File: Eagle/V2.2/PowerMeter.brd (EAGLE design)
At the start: 100 x 80 mm, 59 parts, among them IC1 4067D, IC2 4514D, X1 STEREOJACKSJ1-3525N, X10 STEREOJACK, X11 STEREOJACK, X12 STEREOJACK, X13 STEREOJACK, X14 STEREOJACK, X15 STEREOJACK, X16 STEREOJACK, X2 STEREOJACK, X3 STEREOJACK, X4 STEREOJACK, X5 STEREOJACK, X6 STEREOJACK, X7 STEREOJACK, X8 STEREOJACK, X9 STEREOJACK

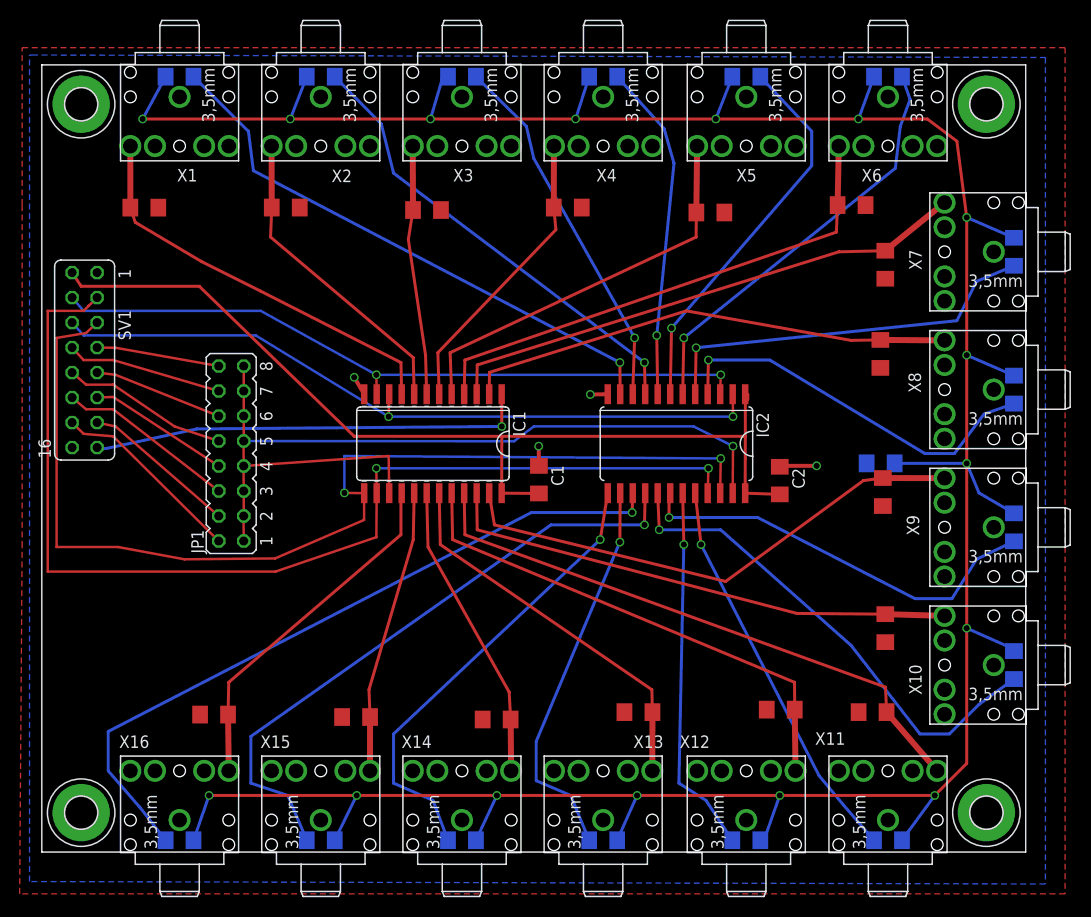
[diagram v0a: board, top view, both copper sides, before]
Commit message: Added V2.2 Eagle files and removed old versions due to hardware bug
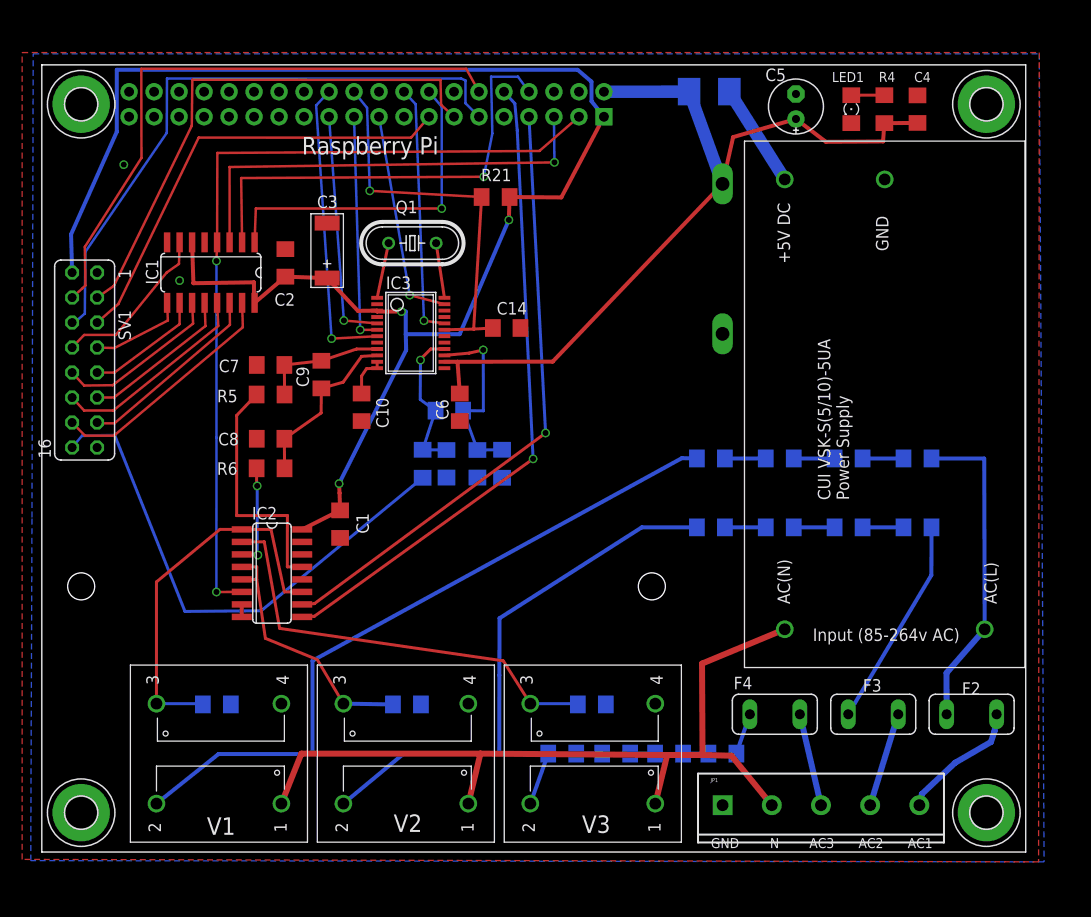
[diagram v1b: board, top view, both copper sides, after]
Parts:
- removed LED10, LED11, LED12, LED13, LED14, LED15, LED16, LED2, LED3, LED4, LED5, LED6, LED7, LED8, LED9: green, eagle-ltspice:LED_1206
- removed X10, X11, X12, X13, X14, X15, X16, X2, X3, X4, X5, X6, X7, X8, X9: STEREOJACK, adafruit:STX3100
- added C10, C14, C4, C6: .1uF, rcl:C1206
- added C11, C12, C7, C8: 220pF, rcl:C1206
- added C13, C9: 22nF, rcl:C1206
- added C3: 10u, Discrete:AVX-C
- added C5: 220uF, adafruit:E2,5-6E
- added D1: P6KE6.8A, diode:C1702-15
- added F1: 1.1A 6V, adafruit:1812
- added F2, F3, F4: MF-RM055/240-2, fuse:TE5
- added IC3: CS5463, Cirrus_Logic_By_element14_Batch_1:SSOP24
- added PS1: VSK-S10, CraigJensen:VSK-S10
- added Q1: 4.096MHz, crystal:HC49/S
- added R18: 59k, resistor:R1206
- added R19, R20: 1k, resistor:R1206
- added R21: 10K, resistor:R1206
- added T1, T2, T3: TV16E, CraigJensen:TV16E
- IC1: value 4067D -> 74HC138D; device 40xx:SO24W -> 74xx-eu:SO16
- IC2: value 4514D -> 4052D; device 45xx:SO24W -> 40xx:SO16
- JP1: value Board ID -> ACIN; device jumper:JP8Q -> SparkFun-Connectors:SCREWTERMINAL-5MM-5
- R1, R2, R3: value 5 -> 158
- R10, R11, R12, R13, R14, R15, R16, R7, R8, R9: value 5 -> 59k
- R17: value 120 -> 59k
- R4: value 5 -> 270
- R5, R6: value 5 -> 1k
- SV1: value (none) -> Current Brd Connector
- X1: value STEREOJACKSJ1-3525N -> RASPI_BOARD_B+_E4; device adafruit:STX3100 -> raspberrypi_bastelstube_v13:RASPI_BOARD_B+_EDGES_4DRILL
- moved H1 92.0 mm to (96.0, 76.0)
- moved H3 92.0 mm to (4.00, 4.00)
- moved X1 77.4 mm to (65.5, 23.5), flipped to the bottom, turned to 0 degrees
- moved R16 74.0 mm to (89.0, 33.0), flipped to the bottom, turned to 0 degrees
- moved H2 72.0 mm to (96.0, 4.00)
- moved H4 72.0 mm to (4.00, 76.0)
- moved LED1 68.3 mm to (82.3, 75.5), flipped to the top, turned to 270 degrees
- moved R6 64.8 mm to (23.2, 39.0), turned to 180 degrees
- moved JP1 62.2 mm to (66.7, 0.30), turned to 0 degrees
- moved C2 54.9 mm to (24.8, 59.9)
- moved R3 53.0 mm to (55.9, 15.0), flipped to the bottom
- moved R2 52.0 mm to (37.1, 15.0), flipped to the bottom
- moved R1 51.0 mm to (17.8, 15.0), flipped to the bottom
- moved R5 48.4 mm to (23.2, 46.5), turned to 180 degrees
- moved IC2 43.2 mm to (23.4, 28.3), turned to 270 degrees
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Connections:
- removed net N$22: IC1.8, R2.1, X2.5
- removed net N$24: IC1.6, R4.1, X4.5
- removed net N$25: IC1.4, R6.1, X6.5
- removed net N$26: IC1.3, R7.1, X7.5
- removed net N$28: IC1.2, R8.1, X8.5
- removed net N$29: IC1.23, R9.1, X9.5
- removed net N$30: IC2.14, LED13.A
- removed net N$32: IC2.19, LED12.A
- removed net N$34: IC2.20, LED11.A
- removed net N$36: IC2.17, LED10.A
- removed net N$40: IC2.4, LED8.A
- removed net N$42: IC2.5, LED7.A
- removed net N$44: IC2.6, LED6.A
- removed net N$48: IC2.8, LED4.A
- removed net N$50: IC1.22, R10.1, X10.5
- removed net N$51: IC1.21, R11.1, X11.5
- removed net N$52: IC2.10, LED3.A
- removed net N$54: IC2.9, LED2.A
- removed net N$56: IC2.11, LED1.A
- removed net N$58: IC1.20, R12.1, X12.5
- removed net N$59: IC1.18, R14.1, X14.5
- removed net N$60: IC1.17, R15.1, X15.5
- removed net N$66: IC1.19, R13.1, X13.5
- removed net N$68: IC1.16, R16.1, X16.5
- removed net VDD: C1.2, C2.2, IC1.24, IC2.1, IC2.24, SV1.2
- new net +3V3: C1.2, C2.2, C3.+, IC1.16, IC1.6, IC2.16, IC3.3, R21.1, SV1.2, X1.1
- new net +5V: F1.2, PS1.P$3
- new net 5V: C4.2, C5.+, C6.2, D1.C, F1.1, IC3.14, R4.1, X1.2
- new net AC(L): F2.1, PS1.P$2, R18.1
- new net AC(N): JP1.2, PS1.P$1, T1.1, T2.1, T3.1
- new net BS-0: IC1.15, SV1.14
- new net BS-1: IC1.14, SV1.13
- new net BS-2: IC1.13, SV1.12
- new net BS-3: IC1.12, SV1.11
- new net BS-4: IC1.11, SV1.10
- new net BS-5: IC1.10, SV1.9
- new net BS-6: IC1.9, SV1.7
- new net BS-7: IC1.7, SV1.8
- new net BS-A: IC1.1, X1.16
- new net BS-B: IC1.2, X1.8
- new net BS-C: IC1.3, X1.5
- new net C5: C12.1, C13.1, IC3.16, R20.2
- new net CS: IC3.7, X1.24
- new net CS-A: SV1.6, X1.11
- new net CS-B: SV1.4, X1.12
- new net CS-C: SV1.3, X1.13
- new net CS-D: SV1.5, X1.15
- new net IIN+: R20.1, SV1.16
- new net INH: IC1.4, IC2.6, X1.3
- new net INT: IC3.20, X1.18
- new net N$39: IC2.3, R6.2
- new net R1: C7.2, C9.2, IC3.9, R5.1
- new net RESET: C14.2, IC3.19, R21.2, X1.22
- new net SCLK: IC3.5, X1.23
- new net SDI: IC3.23, X1.19
- new net SDO: IC3.6, X1.21
- new net VIN-1: IC2.1, IC2.11, R1.2, T1.4
- new net VIN-2: IC2.4, IC2.5, R2.2, T2.4
- new net VIN-3: IC2.2, R3.2, T3.4
- new net VS-A: IC2.10, X1.7
- new net VS-B: IC2.9, X1.10
- net GND: now also C10.1, C11.1, C12.2, C14.1, C3.-, C4.1, C5.-, C6.1, C7.1, C8.2, D1.A, IC1.5, IC1.8, IC2.14, IC2.15, IC2.7, IC2.8, IC3.13, IC3.4, IC3.8, JP1.1, LED1.C, PS1.P$4, R1.1, R19.1, R2.1, R3.1, SV1.15, T1.3, T2.3, T3.3, X1.6; no longer IC1.12, R17.1
- net N$1: now also IC3.1, Q1.1; no longer IC1.10, IC2.2, SV1.6
- net N$10: now also R15.1, R17.2; no longer JP1.6, SV1.12
- net N$11: now also R9.2, T3.2; no longer JP1.2, SV1.14
- net N$12: now also IC3.24, Q1.2; no longer R1.2, R10.2, R11.2, R12.2, R13.2, R14.2, R15.2, R16.2, R2.2, R3.2, R4.2, R5.2, R6.2, R7.2, R8.2, R9.2, SV1.16, X1.1, X1.4, X10.1, X10.4, X11.1, X11.4, X12.1, X12.4, X13.1, X13.4, X14.1, X14.4, X15.1, X15.4, X16.1, X16.4, X2.1, X2.4, X3.1, X3.4, X4.1, X4.4, X5.1, X5.4, X6.1, X6.4, X7.1, X7.4, X8.1, X8.4, X9.1, X9.4
- net N$13: now also R12.2, R9.1; no longer JP1.4, SV1.13
- net N$14: now also R12.1, R15.2; no longer JP1.8, SV1.11
- net N$15: now also R8.2, T2.2; no longer JP1.12, SV1.9
- net N$16: now also R11.2, R8.1; no longer JP1.16, SV1.7
- net N$17: now also C10.2, IC3.11, IC3.12; no longer IC1.1, SV1.15
- net N$18: now also R14.1, R16.2; no longer IC1.5, R5.1, X5.5
- net N$19: now also R7.2, T1.2; no longer IC2.13, LED14.A
- net N$2: now also F3.1, R16.1; no longer IC2.15, LED16.A
- net N$20: now also R13.1, R18.2; no longer IC1.9, R1.1, X1.5
- net N$21: now also F4.1, R17.1; no longer LED1.C, LED10.C, LED11.C, LED12.C, LED13.C, LED14.C, LED15.C, LED16.C, LED2.C, LED3.C, LED4.C, LED5.C, LED6.C, LED7.C, LED8.C, LED9.C, R17.2
- net N$23: now also IC2.13, R5.2; no longer IC1.7, R3.1, X3.5
- net N$3: now also R10.2, R7.1; no longer IC1.11, IC2.3, SV1.4
- net N$38: now also F3.2, JP1.4; no longer IC2.18, LED9.A
- net N$4: now also R10.1, R13.2; no longer IC1.14, IC2.21, SV1.3
- net N$46: now also C8.1, C9.1, IC3.10, R6.1; no longer IC2.7, LED5.A
- net N$5: now also F4.2, JP1.3; no longer IC1.13, IC2.22, SV1.5
- net N$6: now also R11.1, R14.2; no longer IC1.15, IC2.23, JP1.1, JP1.11, JP1.13, JP1.15, JP1.3, JP1.5, JP1.7, JP1.9
- net N$7: now also LED1.A, R4.2; no longer JP1.14, SV1.8
- net N$8: now also C11.2, C13.2, IC3.15, R19.2; no longer JP1.10, SV1.10
- net N$9: now also F2.2, JP1.5; no longer IC2.16, LED15.A
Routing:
- net N$21: track 314.5 -> 4.23 mm, vias 16 -> 0
- net +3V3: track 0.00 -> 167.2 mm, vias 0 -> 3
- net N$4: track 109.3 -> 4.16 mm, vias 2 -> 0
- net VDD: track 99.0 -> 0.00 mm
- net N$5: track 108.3 -> 9.49 mm, vias 2 -> 0
- net N$6: track 92.1 -> 4.16 mm, vias 1 -> 0
- net INH: track 0.00 -> 85.2 mm, vias 0 -> 2
- net AC(N): track 0.00 -> 84.4 mm
- net 5V: track 0.00 -> 84.2 mm
- net N$1: track 74.6 -> 5.68 mm, vias 2 -> 0
- net N$3: track 72.2 -> 4.16 mm, vias 2 -> 0
- net VS-B: track 0.00 -> 66.4 mm, vias 0 -> 1
- net CS-A: track 0.00 -> 62.7 mm
- net VS-A: track 0.00 -> 62.6 mm, vias 0 -> 1
- net CS-B: track 0.00 -> 61.2 mm
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- added copper zone on layer 1, net GND
- removed copper zone on layer 1, net N$12
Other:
- board text added: "AC1"
- board text added: "AC2"
- board text added: "AC3"
- board text added: "GND"
- board text added: "N"
- board text added: "Raspberry Pi"
- board text added: "Raspberry Pi Power Meter V2.2 Craig Jensen 2015"
- board text added: "V1"
- board text added: "V2"
- board text added: "V3"
- board text removed: "Raspberry Pi Power Meter V2.0 Craig Jensen, 2015"
